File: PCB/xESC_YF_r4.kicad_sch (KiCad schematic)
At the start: 32 parts, among them J1 Conn_01x09_Male, J10 OM-MB W => MC BRK, J11 Conn_01x04_Pin, J3 Conn_01x05_Male, J4 Conn_01x05_Male, J6 OM-MB U => MC SA, J7 Conn_01x06_Male, J8 Conn_01x06_Pin, J9 OM-MB V => MC +24V, U1 STM32C011F6Px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

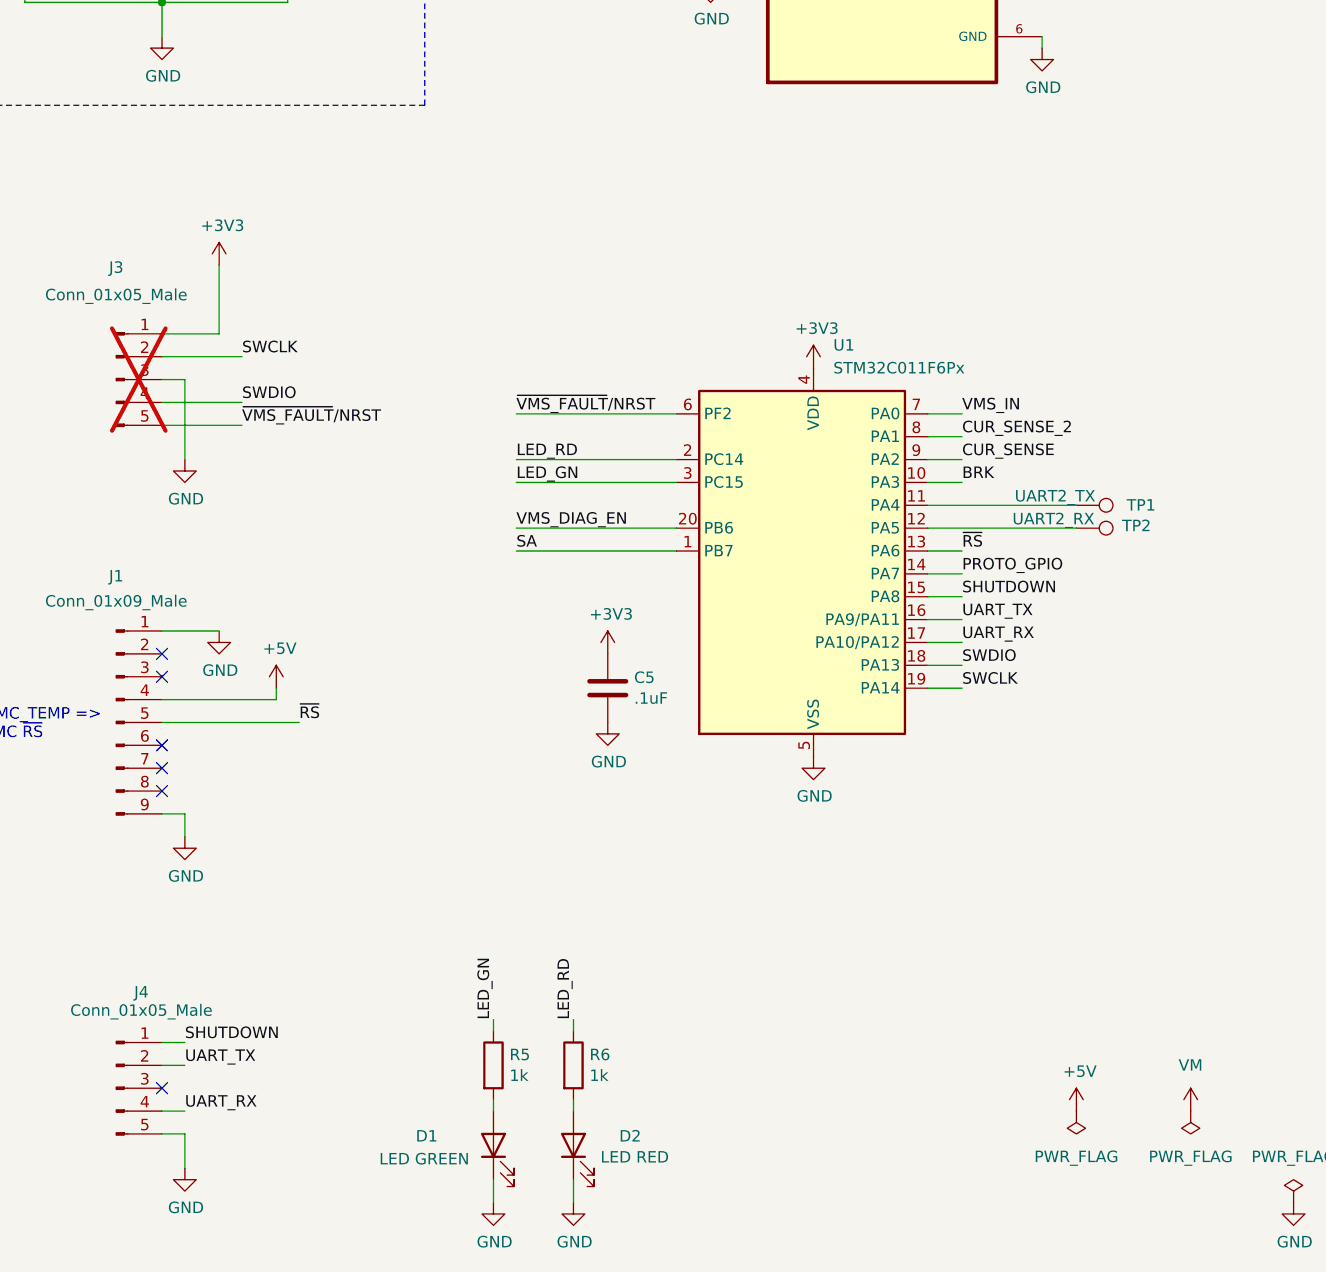
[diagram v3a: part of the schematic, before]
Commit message: UART protection
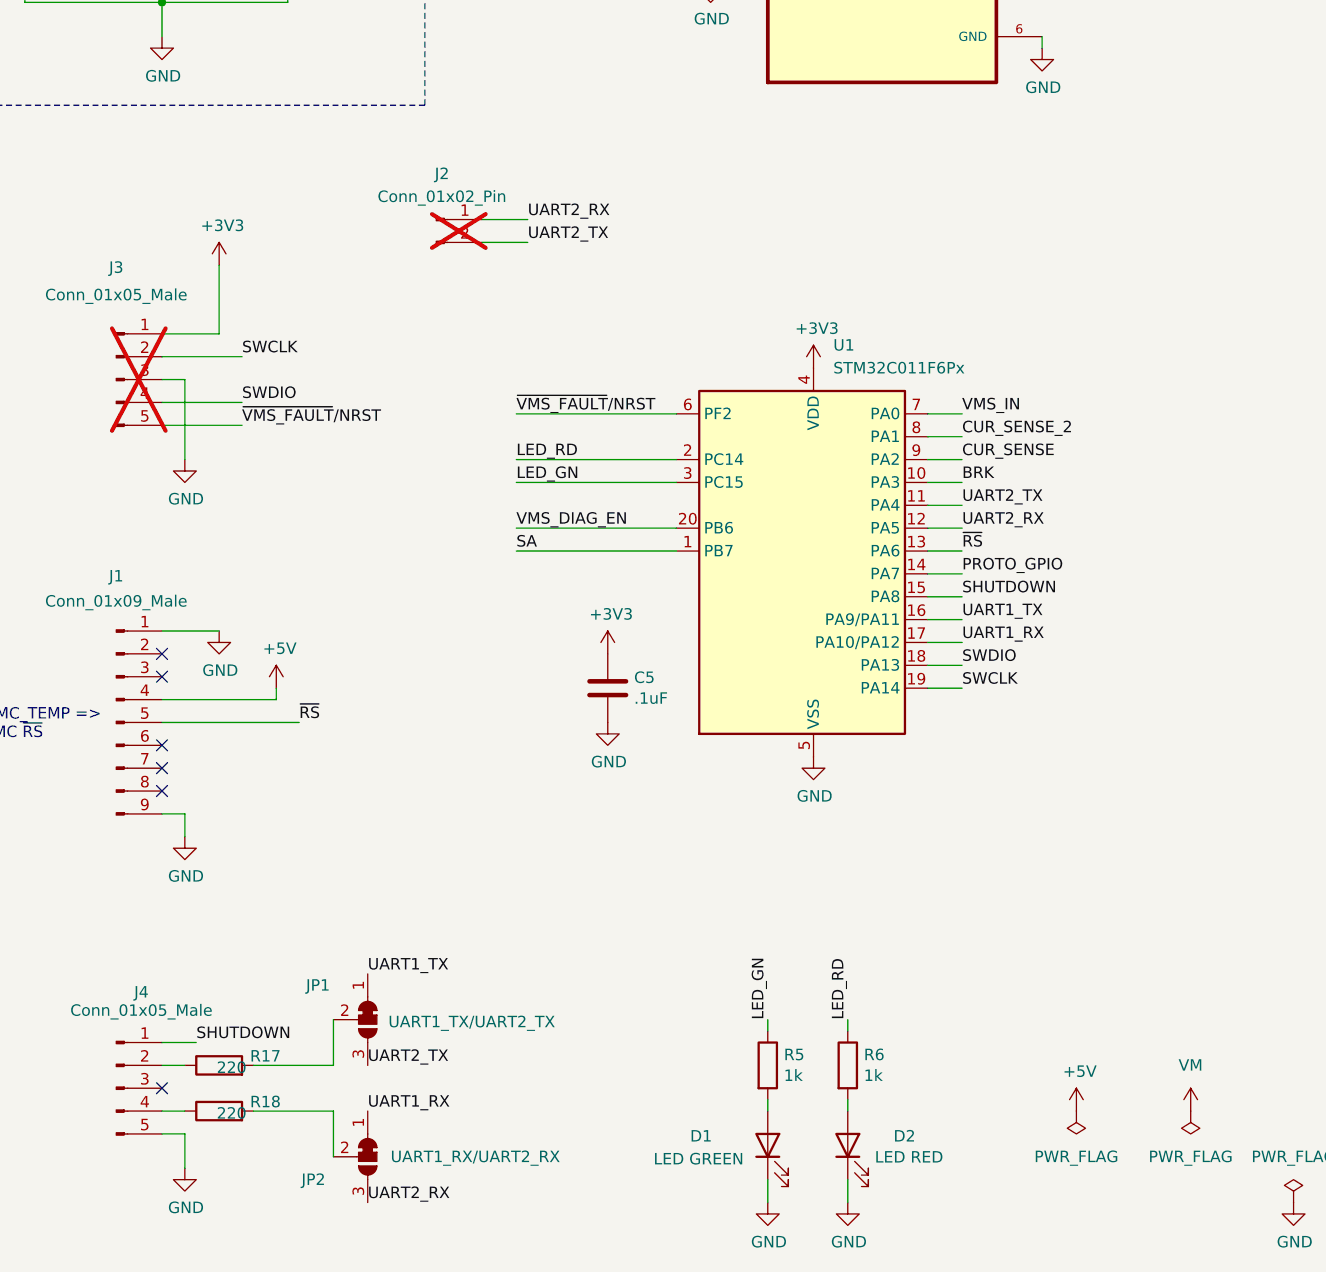
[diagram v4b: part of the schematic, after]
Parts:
- removed TP1: UART2_TX, TestPoint:TestPoint_Pad_1.5x1.5mm, symbol Connector:TestPoint
- removed TP2: UART2_RX, TestPoint:TestPoint_Pad_1.5x1.5mm, symbol Connector:TestPoint
- added J2: Conn_01x02_Pin, Connector_PinHeader_2.54mm:PinHeader_1x02_P2.54mm_Vertical, symbol Connector:Conn_01x02_Pin
- added JP1: UART1_TX/UART2_TX, Jumper:SolderJumper-3_P1.3mm_Bridged12_RoundedPad1.0x1.5mm_NumberLabels, symbol Jumper:SolderJumper_3_Bridged12
- added JP2: UART1_RX/UART2_RX, Jumper:SolderJumper-3_P1.3mm_Bridged12_RoundedPad1.0x1.5mm_NumberLabels, symbol Jumper:SolderJumper_3_Bridged12
- added R17, R18: 220, Resistor_SMD:R_0603_1608Metric, symbol Device:R
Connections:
- net UART2_RX: now reaches U1.12 (PA5)
- net UART2_RX: now also J2.1 (Pin_1), JP2.3 (B)
- net UART2_TX: now reaches U1.11 (PA4)
- net UART2_TX: now also J2.2 (Pin_2), JP1.3 (B)
- net UART_RX: no longer names the net of J4.4 (Pin_4)
- net UART_RX: now also R18.1; no longer U1.17 (PA10/PA12)
- net UART_TX: no longer names the net of J4.2 (Pin_2)
- net UART_TX: now also R17.1; no longer U1.16 (PA9/PA11)
- new net: JP2.2 (C), R18.2
- new net: JP1.2 (C), R17.2
- new net UART1_RX: JP2.1 (A), U1.17 (PA10/PA12)
- new net UART1_TX: JP1.1 (A), U1.16 (PA9/PA11)
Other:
- moved on the sheet: D1, D2, R5, R6

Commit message: Cleanup
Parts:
- R5, R6: value 1k -> 150R
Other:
- note added: "(OM-MB MC_TEMP)"
- note removed: "OM-MB MC_TEMP => MC ~{RS}"
- moved on the sheet: C24, C25, C5, D1, D2, J1, J2, J3, J4, J7, J8, JP1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

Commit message: Commissioned
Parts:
- D1: JLCPCB (none) -> KT-0603G
- D2: JLCPCB (none) -> KT-0603R
- R9: value 82mR -> 75mR; footprint Resistor_SMD:R_0805_2012Metric_Pad1.20x1.40mm_HandSolder -> Resistor_SMD:R_2010_5025Metric_Pad1.40x2.65mm_HandSolder; JLCPCB C2442701 -> C333474; Part Number KDV08FR082ET -> RTT20R075FTE; Stock_PN R-0805-.082-0.25W-1% -> R-2010-.075-0.5W-1%
- U1: value STM32C011F6Px -> STM32C011F6P6; JLCPCB (none) -> C5456198
- U2: value TPS1H200A-Q1 -> TPS1H200A; JLCPCB (none) -> C2653785
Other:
- note added: "Current Sense Calculations ---------------------- I_{nom} = 30W/24V = 1.25A V_{shunt} full-scale target = 100mV (max. 500mV) R_{shunt} = 0.1V/1.25A = 80mΩ P_{shunt} = 0.1V*1.25A = 0.125W = 1/8W More common shunt value = 75mΩ V_{shunt} = 75mΩ * 1.25A = 0.09375V P_{shunt} = 0.09375V * 1.25A = 0.117W => 1/4W V_{OUTMAX} = 3.3V - 0.7V - 0.09375V = 2.506V V_{OUT} target = 2V Gain = 21.33 => 20G R_{L} =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"
- note removed: "Current Sense Calculations ---------------------- I_{nom} = 30W/24V = 1.25A V_{shunt} full-scale target = 100mV (max. 500mV) R_{shunt} = 0.1V/1.25A = 80mΩ P_{shunt} = 0.1V*1.25A = 0.125W = 1/8W More common shunt value = 82mΩ V_{shunt} = 82mΩ * 1.25A = 0.1025V V_{OUTMAX} = 3.3V - 0.7V - 0.1025V = 2.4975V V_{OUT} target = 2V Gain = 19.51 => 20G R_{L} = 20kΩ V_{OUT} nom = 1.25A * 0.082Ω * 0.001 * 20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"
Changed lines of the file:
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@@
 		)
 	)
-	(text "Current Sense Calculations\n----------------------\nI_{nom} = 30W/24V = 1.25A\nV_{shunt} full-scale target = 100mV (max. 500mV)\nR_{shunt} = 0.1V/1.25A = 80mΩ\nP_{shunt} = 0.1V*1.25A = 0.125W = 1/8W\n\nMore common shunt value = 82mΩ\nV_{shunt} = 82mΩ * 1.25A = 0.1025V\n\nV_{OUTMAX} = 3.3V - 0.7V - 0.1025V = 2.4975V\nV_{OUT} target = 2V\n\nGain = 19.51 => 20G\nR_{L} = 20kΩ\n\nV_{OUT} nom = 1.25A * 0.082Ω * 0.001 * 20000 = 2.05V\n"
+	(text "Current Sense Calculations\n----------------------\nI_{nom} = 30W/24V = 1.25A\nV_{shunt} full-scale target = 100mV (max. 500mV)\nR_{shunt} = 0.1V/1.25A = 80mΩ\nP_{shunt} = 0.1V*1.25A = 0.125W = 1/8W\n\nMore common shunt value = 75mΩ\nV_{shunt} = 75mΩ * 1.25A = 0.09375V\nP_{shunt} = 0.09375V * 1.25A = 0.117W => 1/4W\n\nV_{OUTMAX} = 3.3V - 0.7V - 0.09375V = 2.506V\nV_{OUT} target = 2V\n\nGain = 21.33 => 20G\nR_{L} = 20kΩ\n\nV_{OUT} nom = 1.25A * 0.075Ω * 0.001 * 20000 = 1.875V\n"
 		(exclude_from_sim no)
 		(at 131.064 97.79 0)
@@
 			)
 		)
+		(property "JLCPCB" "KT-0603G"
+			(at 93.98 179.07 90)
+			(effects
+				(font
+					(size 1.27 1.27)
+				)
+				(hide yes)
+			)
+		)
 		(pin "1"
 		)
@@
 			)
 		)
+		(property "JLCPCB" "KT-0603R"
+			(at 102.87 179.07 90)
+			(effects
+				(font
+					(size 1.27 1.27)
+				)
+				(hide yes)
+			)
+		)
 		(pin "1"
 		)
@@
 			)
 		)
-		(property "Value" "TPS1H200A-Q1"
+		(property "Value" "TPS1H200A"
 			(at 158.75 22.098 0)
 			(effects
@@
 			)
 		)
+		(property "JLCPCB" "C2653785"
+			(at 158.75 41.91 0)
+			(effects
+				(font
+					(size 1.27 1.27)
+				)
+				(hide yes)
+			)
+		)
 		(pin "8"
 		)
@@
 			)
 		)
-		(property "Value" "STM32C011F6Px"
+		(property "Value" "STM32C011F6P6"
 			(at 98.7141 95.25 0)
 			(effects
@@
 			)
 		)
+		(property "JLCPCB" "C5456198"
+			(at 93.98 118.11 0)
+			(effects
+				(font
+					(size 1.27 1.27)
+				)
+				(hide yes)
+			)
+		)
 		(pin "8"
 		)
@@
 			)
 		)
-		(property "Value" "82mR"
+		(property "Value" "75mR"
 			(at 226.9236 82.55 90)
 			(effects
@@
 			)
 		)
-		(property "Footprint" "Resistor_SMD:R_0805_2012Metric_Pad1.20x1.40mm_HandSolder"
+		(property "Footprint" "Resistor_SMD:R_2010_5025Metric_Pad1.40x2.65mm_HandSolder"
 			(at 228.092 82.55 90)
 			(effects
@@
 			)
 		)
-		(property "Stock_PN" "R-0805-.082-0.25W-1%"
+		(property "Stock_PN" "R-2010-.075-0.5W-1%"
 			(at 229.87 82.55 0)
 			(effects
@@
 			)
 		)
-		(property "Part Number" "KDV08FR082ET"
+		(property "Part Number" "RTT20R075FTE"
 			(at 229.87 82.55 0)
 			(effects
@@
 			)
 		)
-		(property "JLCPCB" "C2442701"
+		(property "JLCPCB" "C333474"
 			(at 229.87 82.55 90)
 			(effects

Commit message: Merge branch 'develop'
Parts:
- added Q1, Q2, Q3: BSS138, Package_TO_SOT_SMD:SOT-23, symbol Transistor_FET:BSS138
- added R1: 47k, Resistor_SMD:R_0805_2012Metric_Pad1.20x1.40mm_HandSolder, symbol Device:R
- added R2, R3, R4, R7, R8: 1k, Resistor_SMD:R_0805_2012Metric_Pad1.20x1.40mm_HandSolder, symbol Device:R
- R5, R6: value 150R -> 220; Digikey 311-150HRCT-ND -> 311-220HRCT-ND; Part Number RC0603FR-07150RL -> RC0603FR-07220RL; Stock_PN R-603-150-.1W-1% -> R-603-220-.1W-1%
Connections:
- net +3V3: now also Q1.1 (G), Q2.1 (G), Q3.1 (G), R1.1, R3.1, R7.1
- net +5V: now also R2.1, R4.1, R8.1
- net BRK: now also Q2.2 (S), R3.2
- net BRK_HV: now also Q2.3 (D), R4.2
- net PROTO_SIG_HV: now also Q3.3 (D), R8.2
- net PROTO_SIG_LV: now also Q3.2 (S), R7.2
- net SA: now also Q1.2 (S), R1.2
- net Level Shifter 1/SIGNAL_HV: no longer names the net of R10.1
- net Level Shifter 1/SIGNAL_HV: now also Q1.3 (D), R2.2
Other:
- removed sheet Level Shifter 1
- removed sheet Level Shifter 2
- removed sheet Level Shifter 3
- moved on the sheet: J10

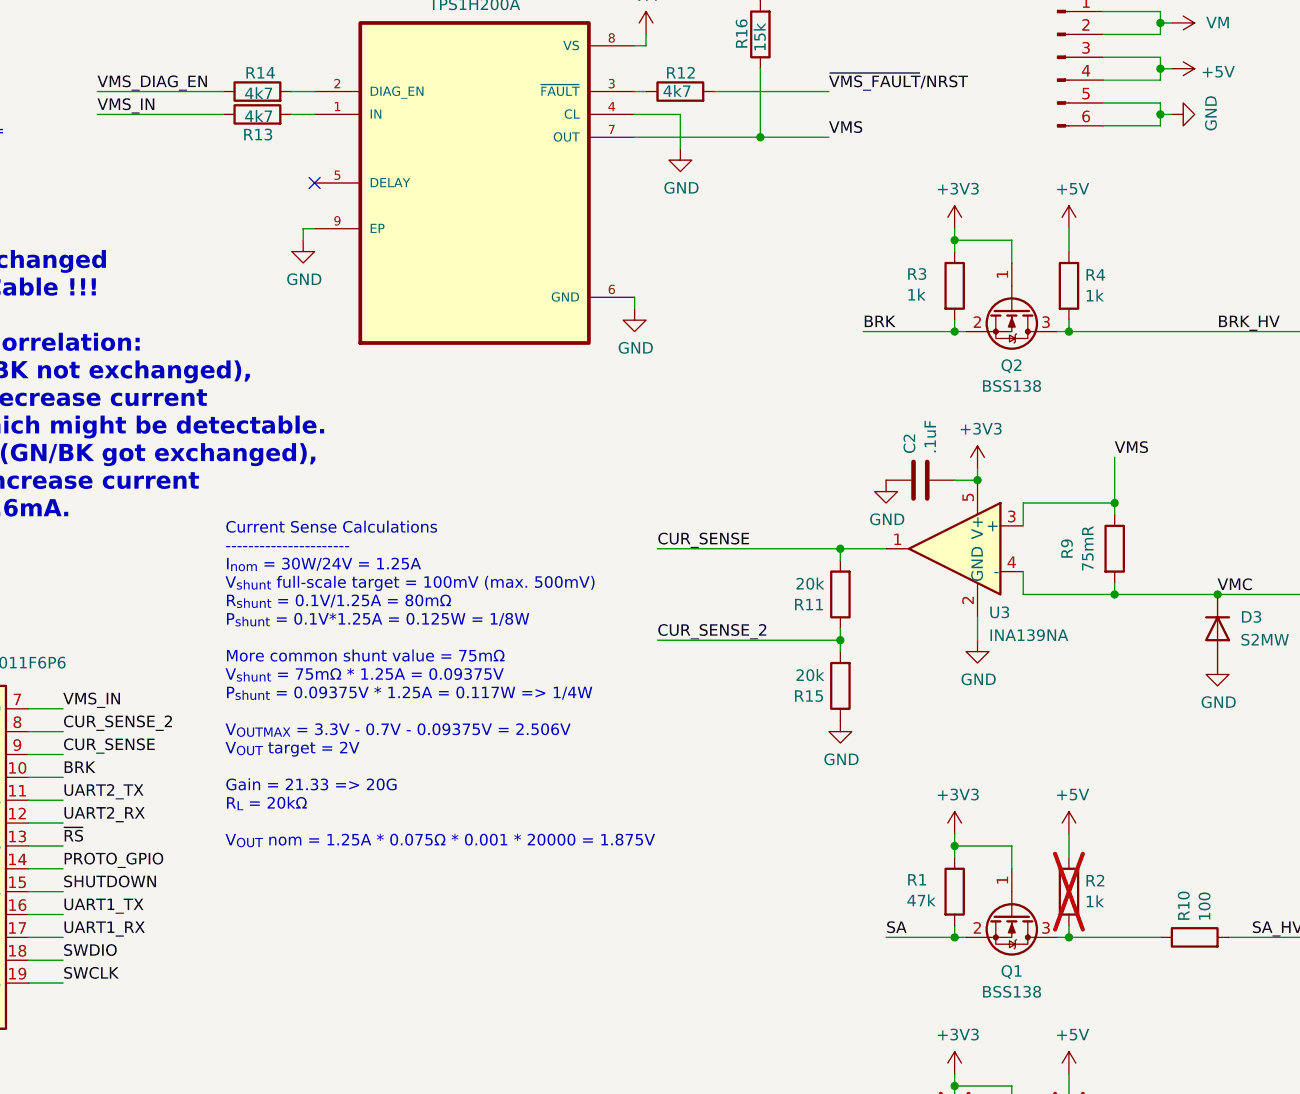
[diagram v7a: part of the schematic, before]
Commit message: Add alternative SA parts
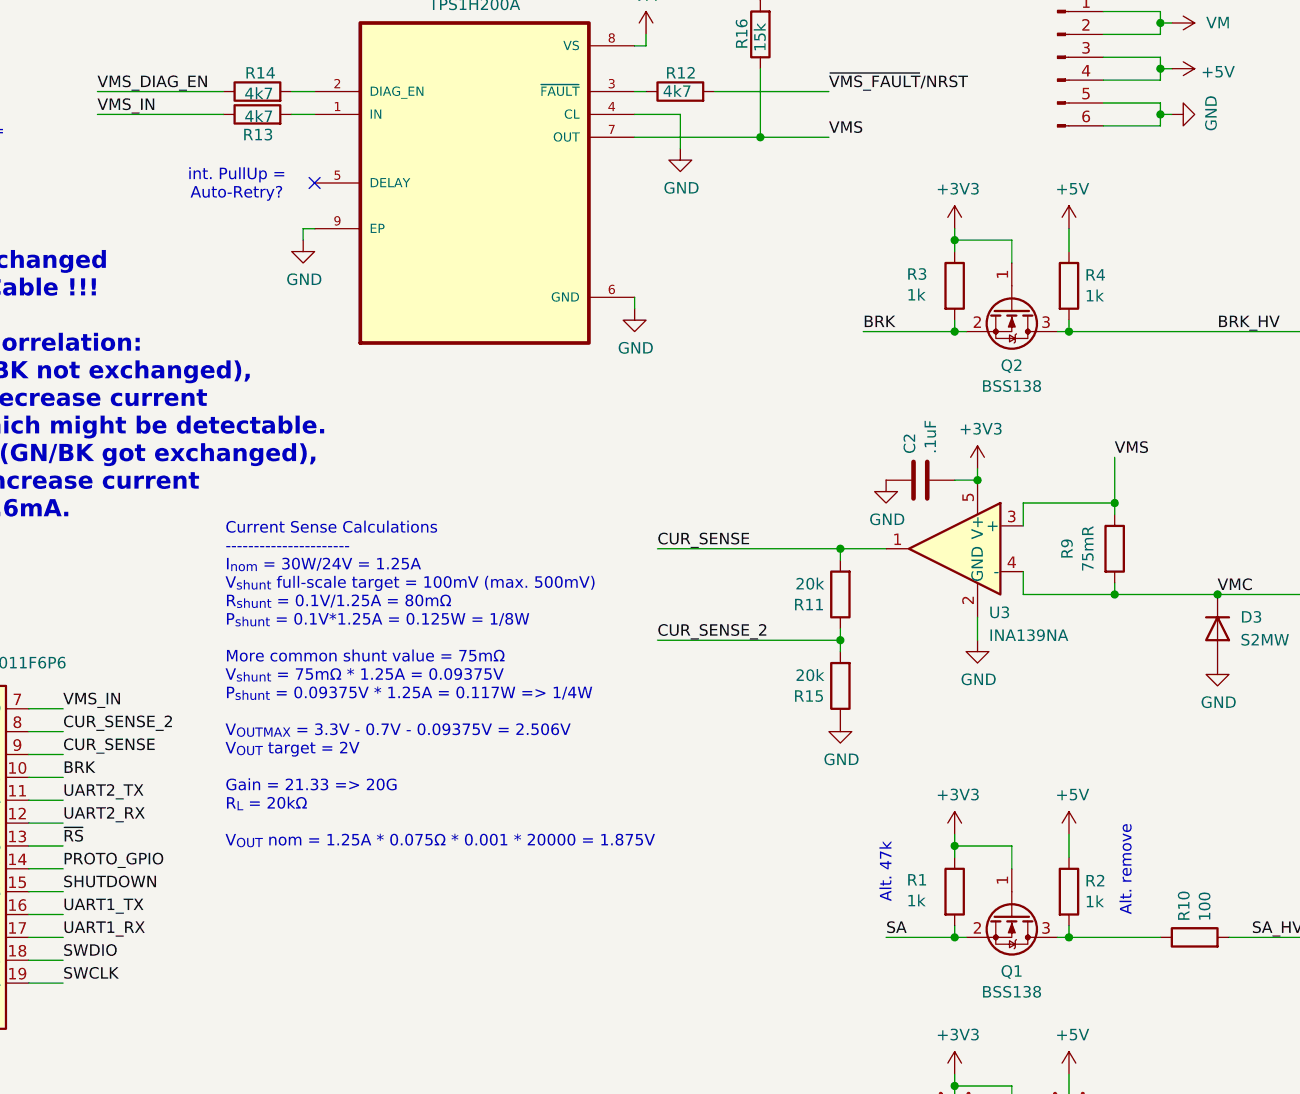
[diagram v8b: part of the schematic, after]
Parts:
- R1: value 47k -> 1k; Stock_PN R-805-47K-.125W-1% -> R-805-1K-.125W-1%
- R2: now fitted; now in the parts list
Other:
- note added: "Alt. 47k"
- note added: "Alt. remove"
- note added: "int. PullUp = Auto-Retry?"
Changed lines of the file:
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@@
 		)
 	)
+	(text "Alt. 47k"
+		(exclude_from_sim no)
+		(at 204.47 118.618 90)
+		(effects
+			(font
+				(size 1.27 1.27)
+			)
+		)
+	)
 	(text "Blade-Motor\nSUMEC Type ??2727, 24VDC, 30W, 3500r/min\n-----------------------------\nRD = +24V\nBK = GND\nGN = SA (SA Hall Output) [TTL] ^{*1}\nYW = ~{RS} (Rotor?-/Rapid?-Start) ^{*2}\nBE = BRK (Break) [Analog] ^{*3}\n\n^{*1}: 1 Cycle = 90°, 4.3ms/Cycle @ 24V =\n   3488 rpm\n^{*2}: Need a new ~{RS} signal after BRK\n^{*3}: As higher the voltage as harder the\n   break (Tested up to 5V)"
 		(exclude_from_sim no)
@@
 		)
 	)
+	(text "int. PullUp =\nAuto-Retry?"
+		(exclude_from_sim no)
+		(at 132.334 42.164 0)
+		(effects
+			(font
+				(size 1.27 1.27)
+			)
+		)
+	)
+	(text "Alt. remove"
+		(exclude_from_sim no)
+		(at 231.14 118.364 90)
+		(effects
+			(font
+				(size 1.27 1.27)
+			)
+		)
+	)
 	(text "!!! GN/BK need to be exchanged \non Mow-Motor-Plug or Cable !!!\n\nDetectable via current correlation:\nWith a wrong plug (GN/BK not exchanged),\npulling SA output to 0 decrease current\nfrom 19mA to 12mA, which might be detectable.\nWhereas a correct plug (GN/BK got exchanged),\npulling SA output to 0 increase current\nonly from 11.3mA to 11.6mA.\n\n"
 		(exclude_from_sim no)
@@
 			)
 		)
-		(property "Value" "47k"
+		(property "Value" "1k"
 			(at 206.756 121.6914 0)
 			(effects
@@
 			)
 		)
-		(property "Stock_PN" "R-805-47K-.125W-1%"
+		(property "Stock_PN" "R-805-1K-.125W-1%"
 			(at 212.09 120.65 0)
 			(effects
@@
 		(unit 1)
 		(exclude_from_sim no)
-		(in_bom no)
+		(in_bom yes)
 		(on_board yes)
-		(dnp yes)
+		(dnp no)
 		(property "Reference" "R2"
 			(at 226.568 119.4816 0)
